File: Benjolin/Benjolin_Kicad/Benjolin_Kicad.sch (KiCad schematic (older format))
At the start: 109 parts, among them P10R 10k, P11R 10k, P1R 10k, P2R 10k, P3R 10k, P4R 10k, P5R 10k, P6R 10k, P8R 10k, P9R 10k, U1 TL074, U2 TL072, U3 TL074, U4 TL074, U5 SSI2164, U6 4021

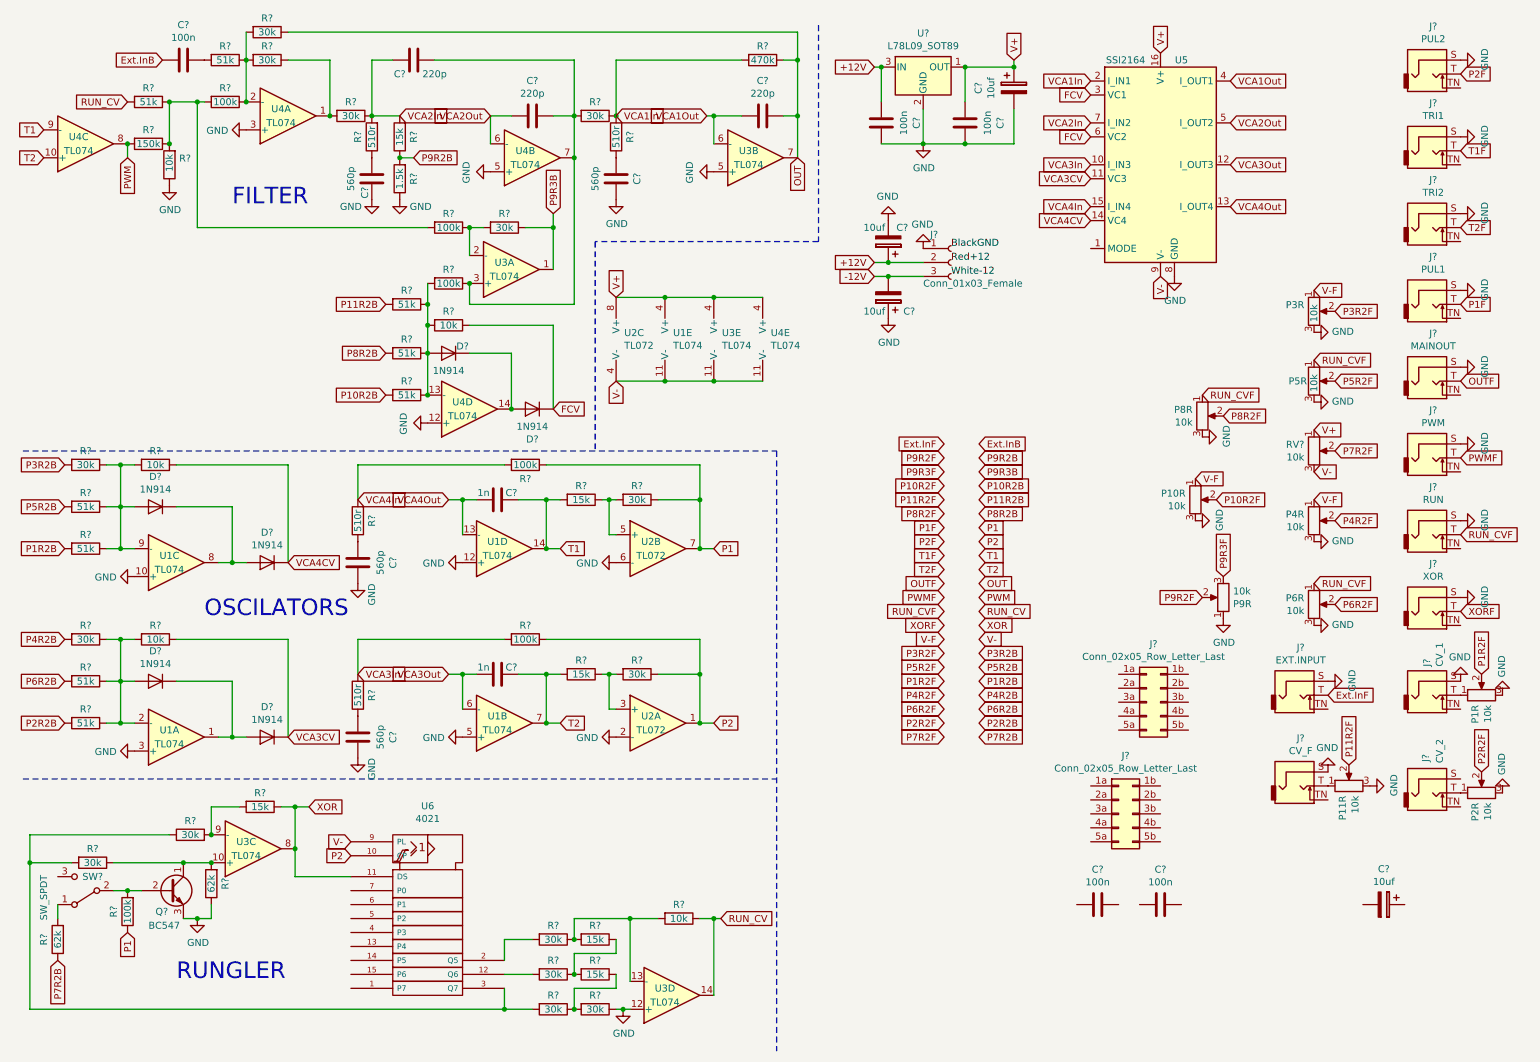
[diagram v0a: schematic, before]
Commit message: Added footprints
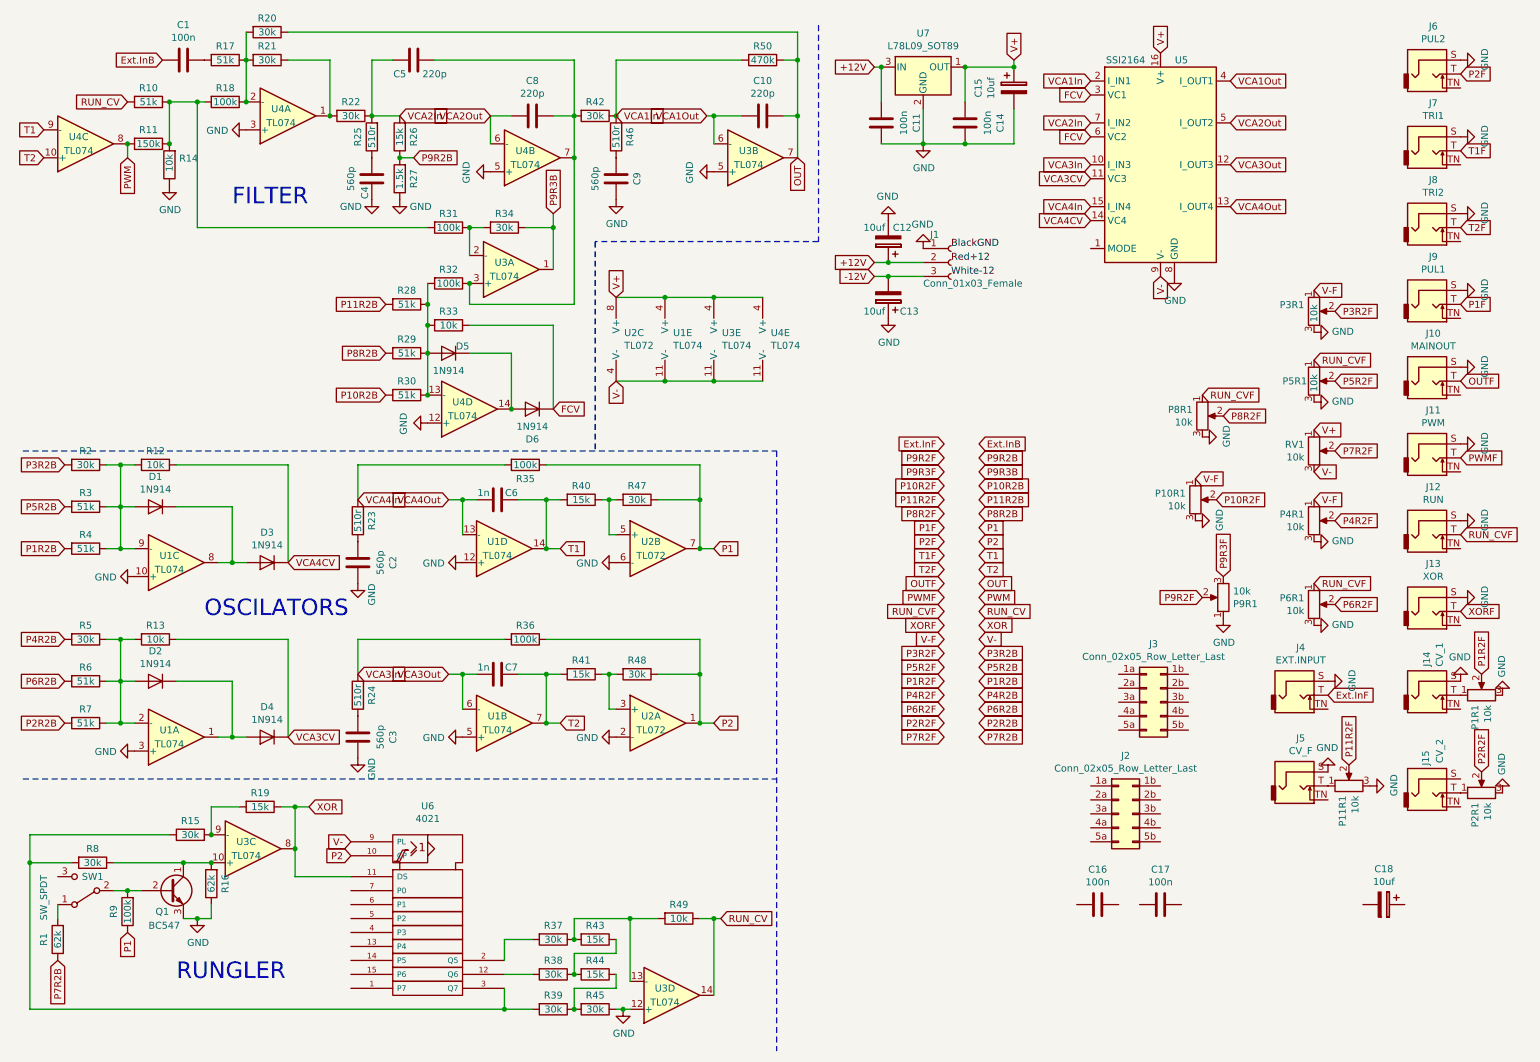
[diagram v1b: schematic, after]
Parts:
- C1, C10, C11, C14, C16, C17, C2, C3, C4, C5, C6, C7, C8, C9: renamed from C?; footprint (none) -> Capacitor_SMD:C_1206_3216Metric_Pad1.42x1.75mm_HandSolder
- C12, C13, C15, C18: renamed from C?; footprint (none) -> Capacitor_THT:CP_Radial_D5.0mm_P2.50mm
- D1, D2, D3, D4, D5, D6: renamed from D?; footprint Diode_THT:D_DO-35_SOD27_P7.62mm_Horizontal -> Diode_THT:D_DO-35_SOD27_P2.54mm_Vertical_AnodeUp
- J1: renamed from J?; footprint (none) -> Connector_PinSocket_2.54mm:PinSocket_1x03_P2.54mm_Vertical
- J10, J11, J12, J13, J14, J15, J4, J5, J6, J7, J8, J9: renamed from J?; footprint (none) -> Connector_Audio:Jack_3.5mm_QingPu_WQP-PJ398SM_Vertical_CircularHoles
- P10R1: renamed from P10R; footprint (none) -> Potentiometer_THT:Potentiometer_Alps_RK09K_Single_Vertical
- P11R1: renamed from P11R; footprint (none) -> Potentiometer_THT:Potentiometer_Alps_RK09K_Single_Vertical
- P1R1: renamed from P1R; footprint (none) -> Potentiometer_THT:Potentiometer_Alps_RK09K_Single_Vertical
- P2R1: renamed from P2R; footprint (none) -> Potentiometer_THT:Potentiometer_Alps_RK09K_Single_Vertical
- P3R1: renamed from P3R; footprint (none) -> Potentiometer_THT:Potentiometer_Alps_RK09K_Single_Vertical
- P4R1: renamed from P4R; footprint (none) -> Potentiometer_THT:Potentiometer_Alps_RK09K_Single_Vertical
- P5R1: renamed from P5R; footprint (none) -> Potentiometer_THT:Potentiometer_Alps_RK09K_Single_Vertical
- P6R1: renamed from P6R; footprint (none) -> Potentiometer_THT:Potentiometer_Alps_RK09K_Single_Vertical
- P8R1: renamed from P8R; footprint (none) -> Potentiometer_THT:Potentiometer_Alps_RK09K_Single_Vertical
- P9R1: renamed from P9R; footprint (none) -> Potentiometer_THT:Potentiometer_Alps_RK09K_Single_Vertical
- R1, R10, R11, R12, R13, R14, R15, R16, R17, R18, R19, R2, R20, R21, R22, R23, R24, R25, R26, R27, R28, R29, R3, R30, R31, R32, R33, R34, R35, R36, R37, R38, R39, R4, R40, R41, R42, R43, R44, R45, R46, R47, R48, R49, R5, R50, R6, R7, R8, R9: renamed from R?; footprint (none) -> Resistor_SMD:R_0603_1608Metric_Pad1.05x0.95mm_HandSolder
- SW1: renamed from SW?; footprint (none) -> Connector_PinSocket_2.54mm:PinSocket_1x03_P2.54mm_Vertical
- U1, U3, U4: footprint (none) -> Package_SO:SOIC-14_3.9x8.7mm_P1.27mm
- U2: footprint (none) -> Package_SO:SOIC-8_3.9x4.9mm_P1.27mm
- U6: footprint (none) -> Package_SO:SOIC-16_3.9x9.9mm_P1.27mm
- U7: renamed from U?; footprint Package_TO_SOT_SMD:SOT-89-3 -> Package_TO_SOT_THT:TO-92L_Inline
- gave numbers to parts that had none: 4
